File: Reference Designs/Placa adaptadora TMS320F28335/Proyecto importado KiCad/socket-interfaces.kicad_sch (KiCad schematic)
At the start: 23 parts, among them J7 DIMM100, P10 Header GPIO, P5 Header 7X2, P6 Header UART, P7 Header I2C, P8 Header PWM, P9 Header ADC, SW1 Switch, SW2 Switch, SW3 Switch, SW4 Switch

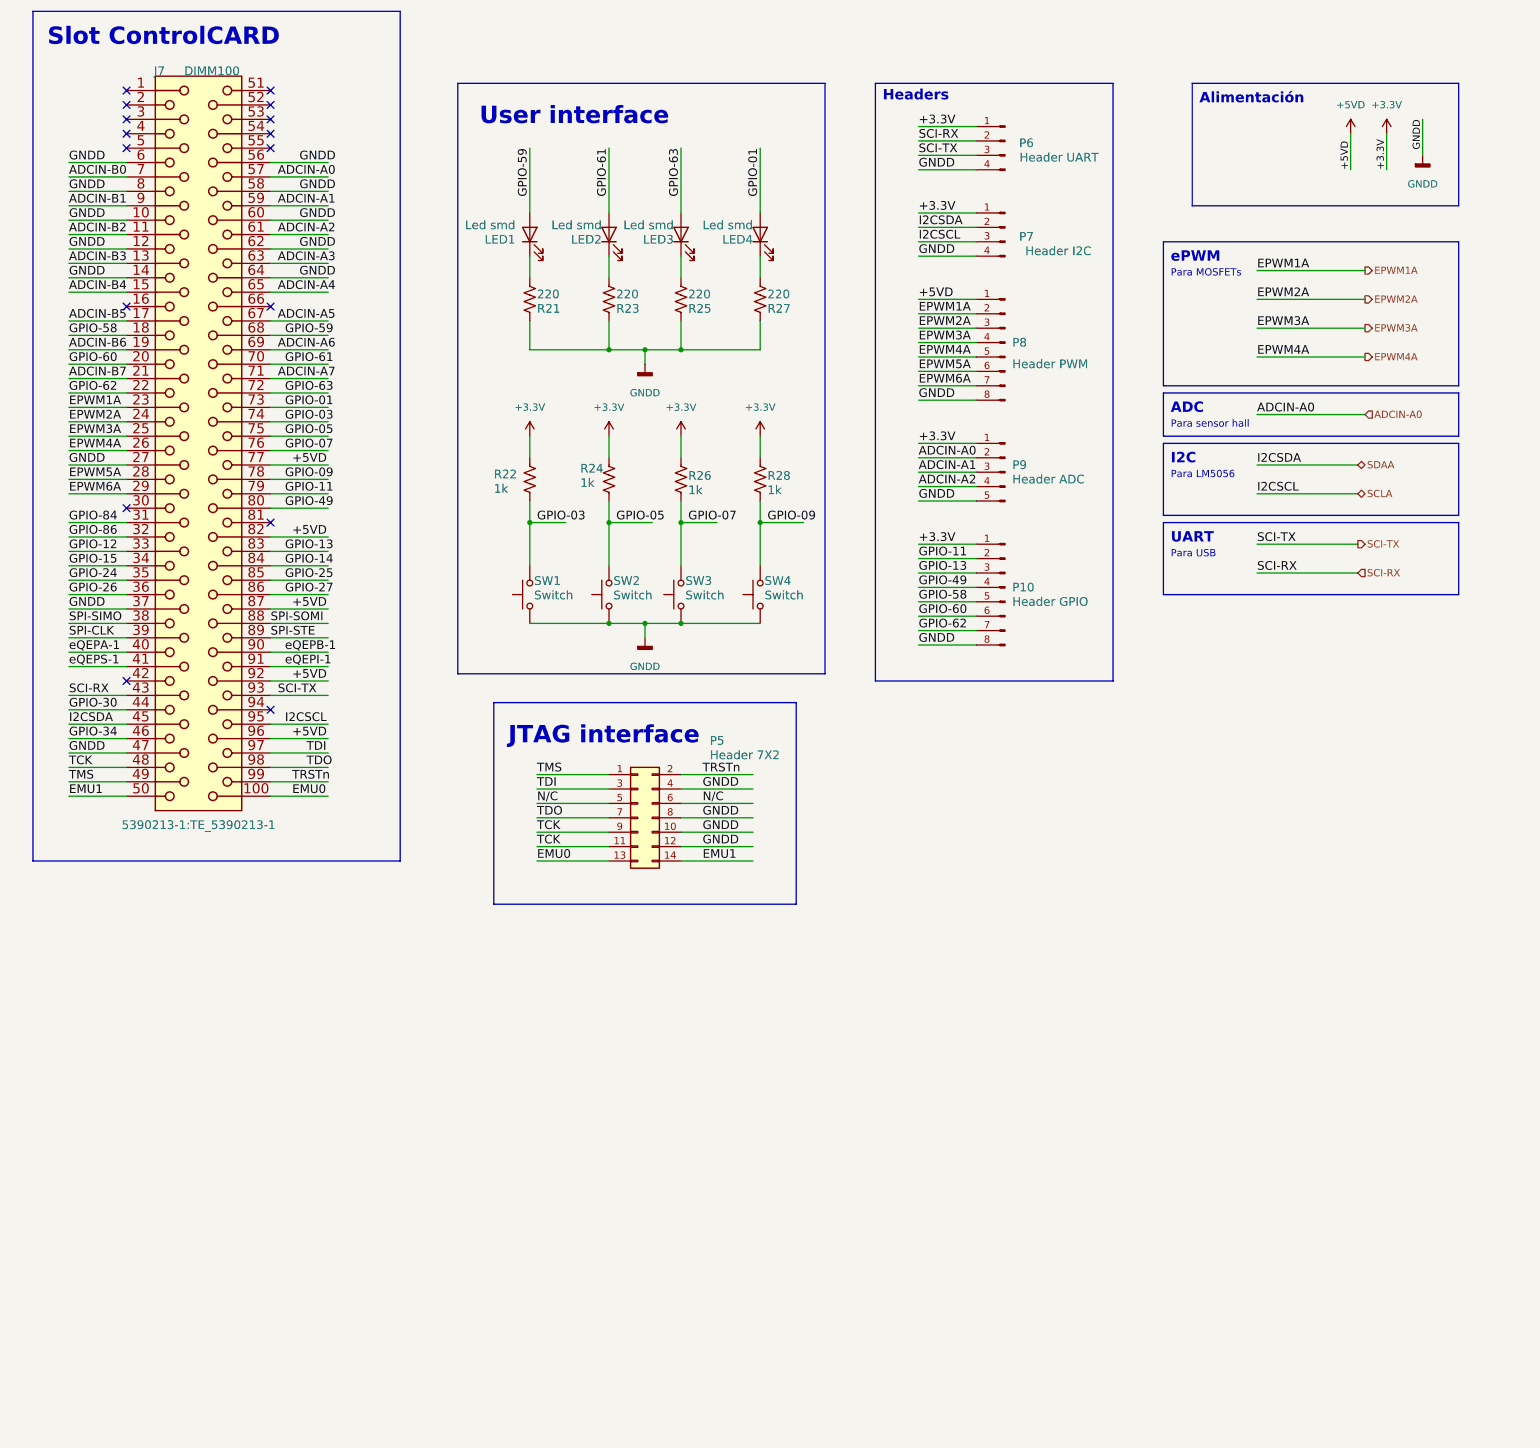
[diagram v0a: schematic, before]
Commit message: Arreglar todos los errores del ERC
- Agregar flags de 'Not Connected' a pines flotantes
- Agregar resistencias 'falsas' para eliminar los errores de 'Power
input pin not connected to Power output pin'
- Agregar un GND1 conectado a PWR_FLAG para arreglar errores
- Además, agregar bien al proyecto la placa adaptadora importada a KiCad
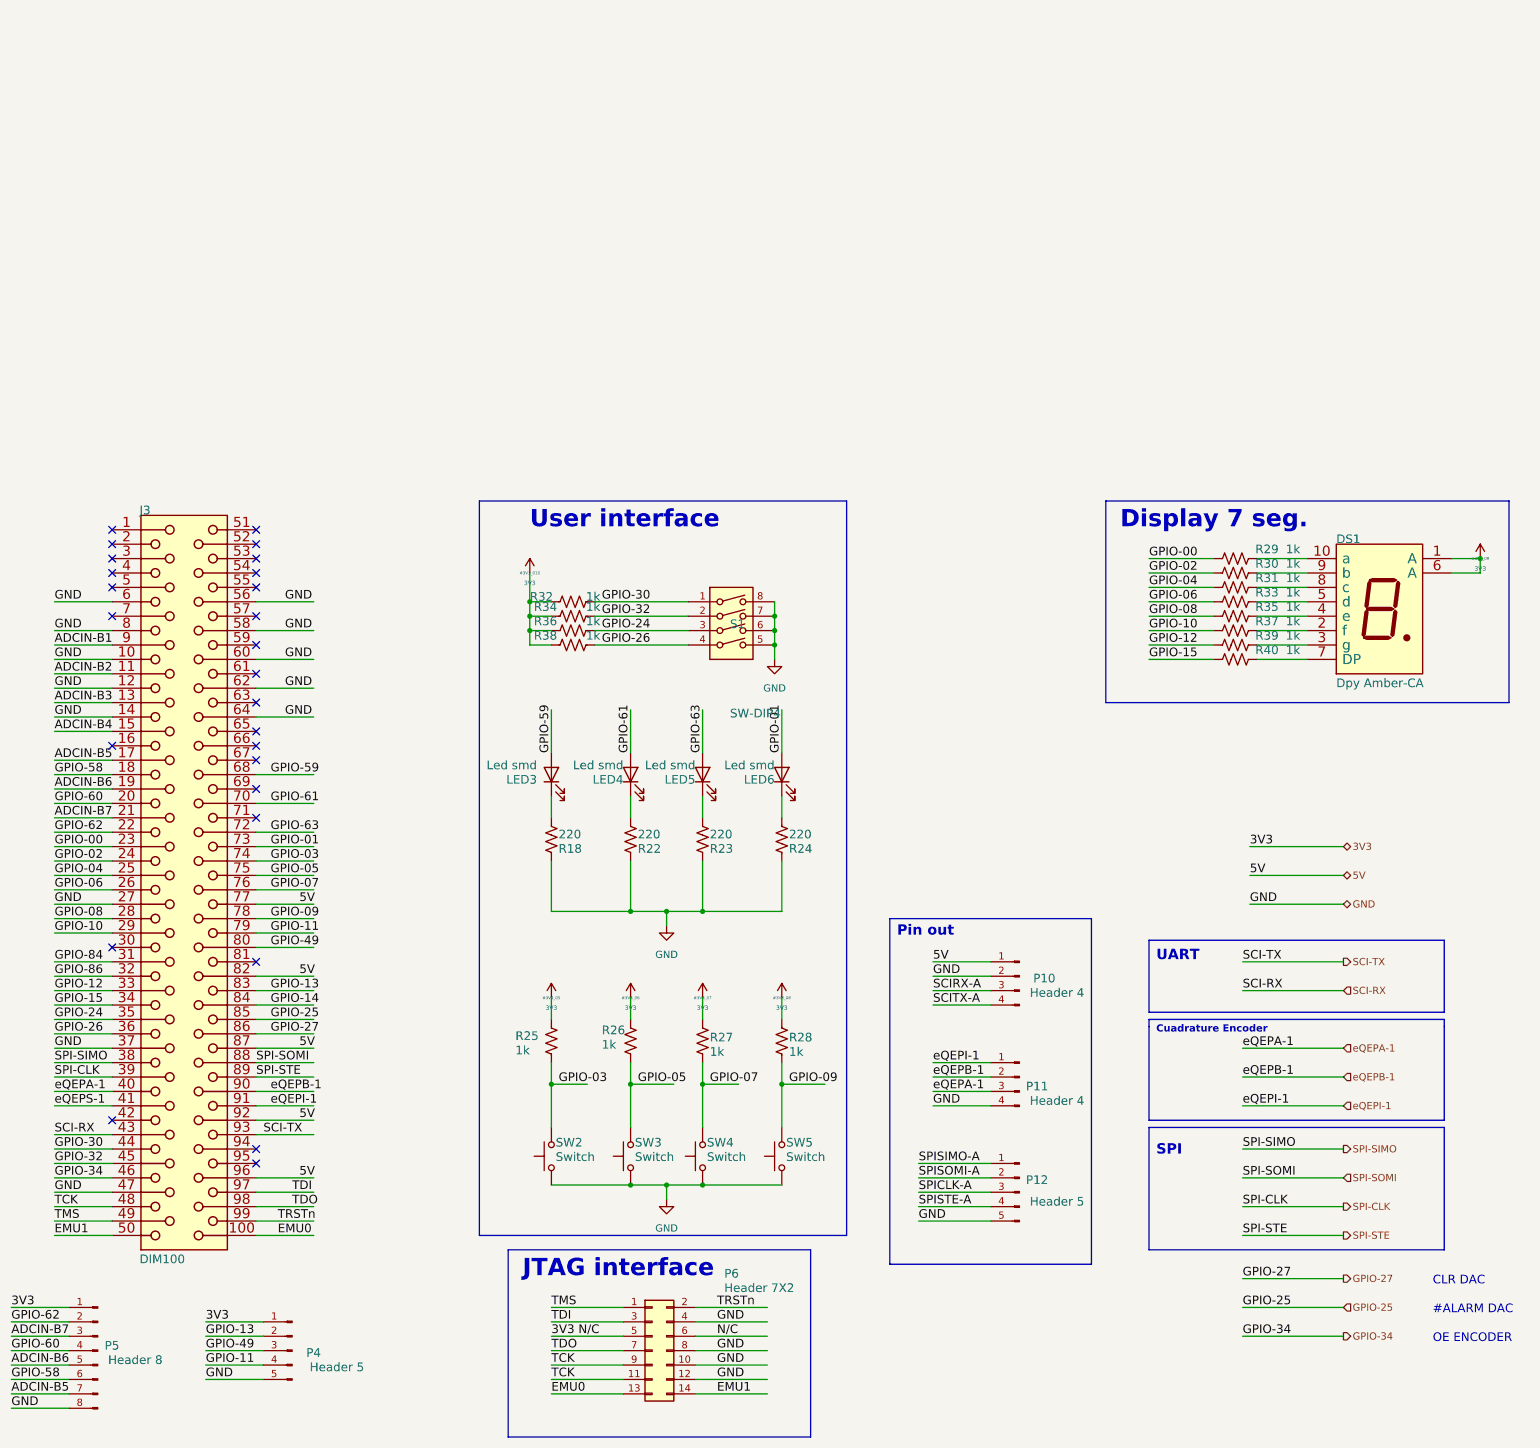
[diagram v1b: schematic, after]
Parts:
- removed J7: DIMM100, 5390213-1:TE_5390213-1, symbol DIMM100:390213-1-
- removed LED1, LED2: Led smd, symbol Device:LED
- removed P10: Header GPIO, symbol Connector:Conn_01x08_Male
- removed P5: Header 7X2, symbol Connector_Generic:Conn_02x07_Odd_Even
- removed P6: Header UART, symbol Connector:Conn_01x04_Male
- removed P7: Header I2C, symbol Connector:Conn_01x04_Male
- removed P8: Header PWM, symbol Connector:Conn_01x08_Male
- removed P9: Header ADC, symbol Connector:Conn_01x05_Male
- removed R21: 220, symbol Device:R_US
- removed SW1: Switch, symbol Switch:SW_Push
- added DS1: Dpy Amber-CA, symbol dpy_amber-ca:Dpy_Amber-CA-
- added J3: DIM100, symbol DIMM100:390213-1-
- added LED5, LED6: Led smd, symbol Device:LED
- added P10, P11: Header 4, symbol Connector:Conn_01x04_Male
- added P12, P4: Header 5, symbol Connector:Conn_01x05_Male
- added P5: Header 8, symbol Connector:Conn_01x08_Male
- added P6: Header 7X2, symbol Connector_Generic:Conn_02x07_Odd_Even
- added R18: 220, symbol Device:R_US
- added R29, R30, R31, R32, R33, R34, R35, R36, R37, R38, R39, R40: 1k, symbol Device:R_US
- added S1: SW-DIP4, symbol Switch:SW_DIP_x04
- added SW5: Switch, symbol Switch:SW_Push
- R22, R24: value 1k -> 220
- R25, R27: value 220 -> 1k
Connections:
- net +3V3: now also R25.2, R27.2, DS1.1 (A), DS1.6 (A), R32.2, R34.1, R36.1, R38.1; no longer R22.2, R24.2
- net ADCIN-B1: now also J3.9 (p9)
- net ADCIN-B2: now also J3.11 (p11)
- net ADCIN-B3: now also J3.13 (p13)
- net ADCIN-B4: now also J3.15 (p15)
- net ADCIN-B5: now also J3.17 (p17), P5.7 (Pin_7)
- net ADCIN-B6: now also J3.19 (p19), P5.5 (Pin_5)
- net ADCIN-B7: now also J3.21 (p21), P5.3 (Pin_3)
- net EMU0: now also J3.100 (p100), P6.13 (Pin_13)
- net EMU1: now also J3.50 (p50), P6.14 (Pin_14)
- net GPIO-01: now also J3.73 (p73), LED6.2 (A); no longer LED4.2 (A)
- net GPIO-03: now also R25.1, SW2.2, J3.74 (p74); no longer R22.1
- net GPIO-05: now also R26.1, SW3.2, J3.75 (p75); no longer R24.1, SW2.2
- net GPIO-07: now also R27.1, SW4.2, J3.76 (p76); no longer R26.1, SW3.2
- net GPIO-09: now also J3.78 (p78), SW5.2; no longer SW4.2
- net GPIO-11: now also J3.79 (p79), P4.4 (Pin_4)
- net GPIO-12: now also J3.33 (p33), R39.1
- net GPIO-13: now also J3.83 (p83), P4.2 (Pin_2)
- net GPIO-14: now also J3.84 (p84)
- net GPIO-15: now also J3.34 (p34), R40.1
- net GPIO-24: now also J3.35 (p35), R36.2, S1.3
- net GPIO-25: now also J3.85 (p85)
- net GPIO-26: now also J3.36 (p36), R38.2, S1.4
- net GPIO-27: now also J3.86 (p86)
- net GPIO-30: now also J3.44 (p44), R32.1, S1.1
- net GPIO-34: now also J3.46 (p46)
- net GPIO-49: now also J3.80 (p80), P4.3 (Pin_3)
- net GPIO-58: now also J3.18 (p18), P5.6 (Pin_6)
- net GPIO-59: now also LED3.2 (A), J3.68 (p68)
- net GPIO-60: now also J3.20 (p20), P5.4 (Pin_4)
- net GPIO-61: now also LED4.2 (A), J3.70 (p70)
- net GPIO-62: now also J3.22 (p22), P5.2 (Pin_2)
- net GPIO-63: now also J3.72 (p72), LED5.2 (A); no longer LED3.2 (A)
- net GPIO-84: now also J3.31 (p31)
- net GPIO-86: now also J3.32 (p32)
- net N/C: now also P6.6 (Pin_6)
- net SCI-RX: now also J3.43 (p43)
- net SCI-TX: now also J3.93 (p93)
- net SPI-CLK: now also J3.39 (p39)
- net SPI-SIMO: now also J3.38 (p38)
- net SPI-SOMI: now also J3.88 (p88)
- net SPI-STE: now also J3.89 (p89)
- net TCK: now also J3.48 (p48), P6.11 (Pin_11), P6.9 (Pin_9)
- net TDI: now also J3.97 (p97), P6.3 (Pin_3)
- net TDO: now also J3.98 (p98), P6.7 (Pin_7)
- net TMS: now also J3.49 (p49), P6.1 (Pin_1)
- net TRSTn: now also J3.99 (p99), P6.2 (Pin_2)
- net eQEPA-1: now also J3.40 (p40), P11.3 (Pin_3)
- net eQEPB-1: now also J3.90 (p90), P11.2 (Pin_2)
- net eQEPI-1: now also J3.91 (p91), P11.1 (Pin_1)
- net eQEPS-1: now also J3.41 (p41)
- net at R23.1: now also LED5.1 (K)
- net at LED4.1 (K): now also R22.1; no longer R27.1
- net at LED3.1 (K): now also R18.1; no longer R25.1
- net GNDD renamed GND
- net GND: now also R22.2, R24.2, J3.10 (p10), J3.12 (p12), J3.14 (p14), J3.27 (p27), J3.37 (p37), J3.47 (p47), J3.56 (p56), J3.58 (p58), J3.6 (p6), J3.60 (p60), J3.62 (p62), J3.64 (p64), J3.8 (p8), P10.2 (Pin_2), P11.4 (Pin_4), P12.5 (Pin_5), P4.5 (Pin_5), P5.8 (Pin_8), P6.10 (Pin_10), P6.12 (Pin_12), P6.4 (Pin_4), P6.8 (Pin_8), R18.2, S1.5, S1.6, S1.7, S1.8, SW5.1; no longer R25.2, R27.2
- new net: DS1.7 (DP), R40.2
- new net: DS1.3 (g), R39.2
- new net: DS1.2 (f), R37.2
- new net: DS1.4 (e), R35.2
- new net: DS1.5 (d), R33.2
- new net: DS1.8 (c), R31.2
- new net: DS1.9 (b), R30.2
- new net: DS1.10 (a), R29.2
- new net: LED6.1 (K), R24.1
- new net 3V3: P4.1 (Pin_1), P5.1 (Pin_1)
- new net 3V3 N/C: P6.5 (Pin_5)
- new net 5V: J3.77 (p77), J3.82 (p82), J3.87 (p87), J3.92 (p92), J3.96 (p96), P10.1 (Pin_1)
- new net GPIO-00: J3.23 (p23), R29.1
- new net GPIO-02: J3.24 (p24), R30.1
- new net GPIO-04: J3.25 (p25), R31.1
- new net GPIO-06: J3.26 (p26), R33.1
- new net GPIO-08: J3.28 (p28), R35.1
- new net GPIO-10: J3.29 (p29), R37.1
- new net GPIO-32: J3.45 (p45), R34.2, S1.2
- new net SCIRX-A: P10.3 (Pin_3)
- new net SCITX-A: P10.4 (Pin_4)
- new net SPICLK-A: P12.3 (Pin_3)
- new net SPISIMO-A: P12.1 (Pin_1)
- new net SPISOMI-A: P12.2 (Pin_2)
- new net SPISTE-A: P12.4 (Pin_4)
- no-connect marks 16 -> 26
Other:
- note added: "#ALARM DAC"
- note added: "CLR DAC"
- note added: "Cuadrature Encoder"
- note added: "Display 7 seg."
- note added: "OE ENCODER"
- note added: "Pin out"
- note added: "SPI"
- note removed: "ADC"
- note removed: "Alimentación"
- note removed: "Headers"
- note removed: "I2C"
- note removed: "Para LM5056"
- note removed: "Para MOSFETs"
- note removed: "Para USB"
- note removed: "Para sensor hall"
- note removed: "Slot ControlCARD"
- note removed: "ePWM"
- title: (none) -> Socket and interfaces
